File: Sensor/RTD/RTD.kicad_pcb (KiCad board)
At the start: 2 copper layers, 28.6 x 26 mm, 17 parts, among them J1 Conn_02x04_Odd_Even, J2 Conn_01x04_Female, U1 MIC5225, U2 MAX31865

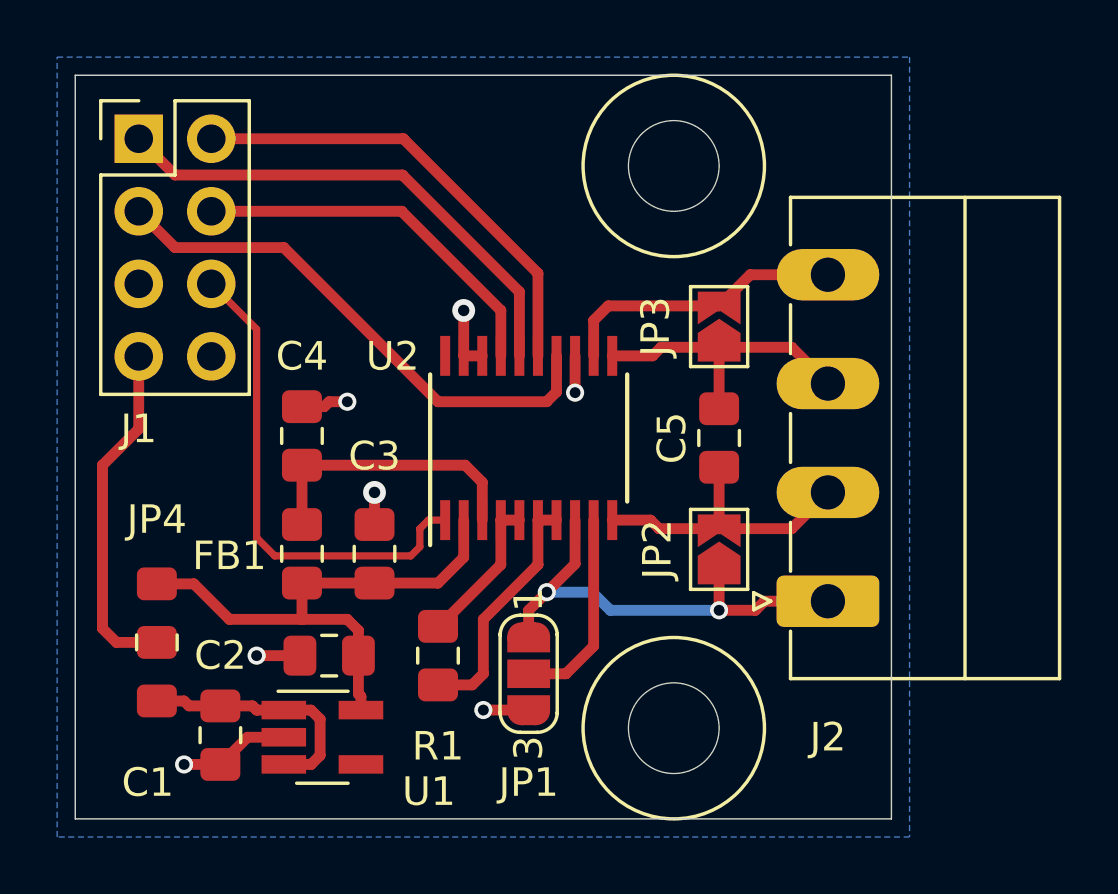
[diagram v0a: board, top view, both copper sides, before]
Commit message: Fix footprint.  Fix wiring for connector.
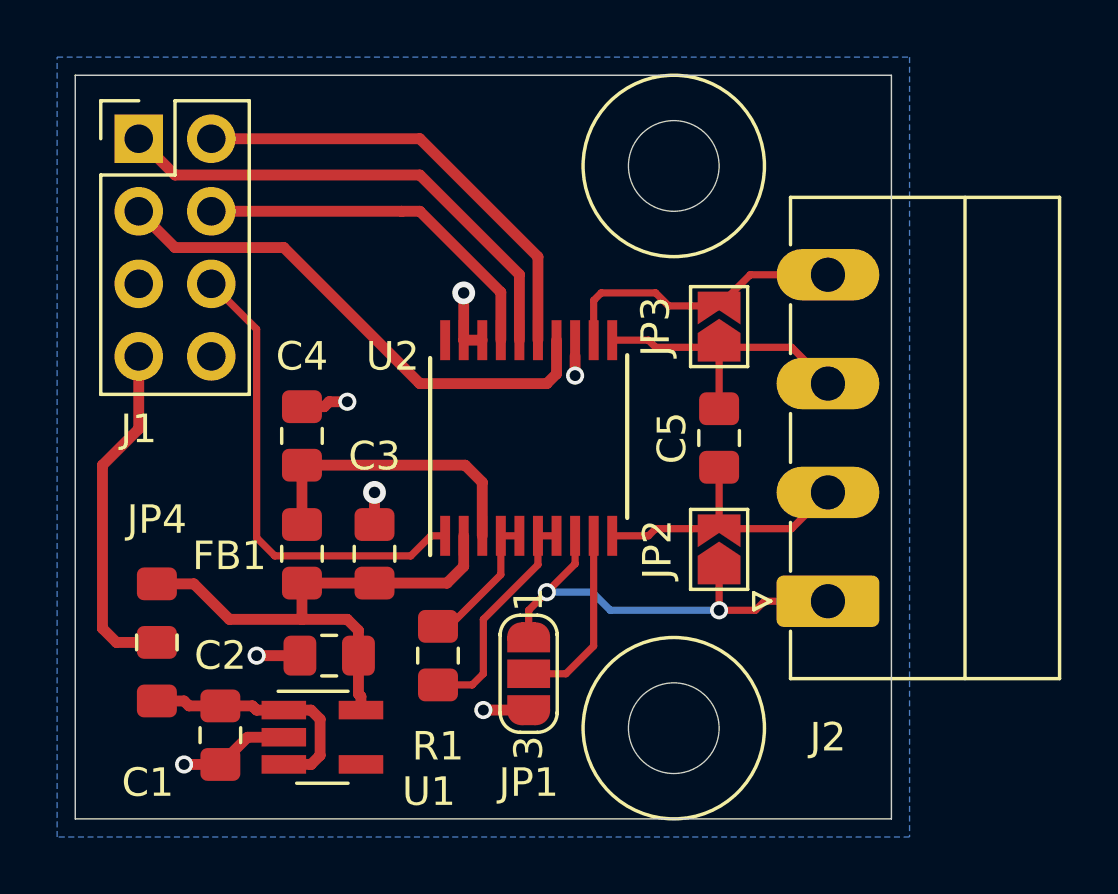
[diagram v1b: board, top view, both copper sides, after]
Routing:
- net /~DRDY: track 17.3 -> 16.7 mm
- net /Vdd: track 9.96 -> 10.5 mm
- net /Force2: track 7.09 -> 6.54 mm
- net /Force+: track 16.4 -> 15.8 mm
- net /Ref-: track 8.57 -> 8.02 mm
- net GND: track 13.3 -> 12.8 mm

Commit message: Updates while making boards.
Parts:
- R1: value R -> 400
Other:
- board text added: "CS SDI NC Vin"
- board text added: "SCLK SDO DRDY GND"
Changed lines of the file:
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@@
   (general
     (thickness 1.6)
-    (drawings 9)
+    (drawings 11)
     (tracks 127)
     (zones 0)
@@
     (pcb_text_size 1.5 1.5)
     (mod_edge_width 0.12)
-    (mod_text_size 1 1)
-    (mod_text_width 0.15)
+    (mod_text_size 0.8 0.8)
+    (mod_text_width 0.12)
     (pad_size 1.524 1.524)
     (pad_drill 0.762)
@@
     (attr smd)
     (fp_text reference U2 (at 2.8575 -4.7625 180) (layer F.SilkS)
-      (effects (font (size 1 1) (thickness 0.15)))
+      (effects (font (size 0.8 0.8) (thickness 0.12)))
     )
     (fp_text value MAX31865 (at 0 4.3 90) (layer F.Fab)
       (effects (font (size 1 1) (thickness 0.15)))
     )
-    (fp_text user %R (at 0 0 90) (layer F.Fab)
-      (effects (font (size 0.8 0.8) (thickness 0.15)))
-    )
-    (fp_line (start -4.1 -3.45) (end 2.8 -3.45) (layer F.SilkS) (width 0.15))
-    (fp_line (start -2.8 3.45) (end 2.9 3.45) (layer F.SilkS) (width 0.15))
+    (fp_line (start -4.1 -3.45) (end 2.8 -3.45) (layer F.SilkS) (width 0.12))
+    (fp_line (start -2.8 3.45) (end 2.9 3.45) (layer F.SilkS) (width 0.12))
     (fp_line (start -4.5 3.55) (end 4.5 3.55) (layer F.CrtYd) (width 0.05))
     (fp_line (start -4.5 -3.55) (end 4.5 -3.55) (layer F.CrtYd) (width 0.05))
@@
     (fp_line (start -1.7 -3.25) (end 2.75 -3.25) (layer F.Fab) (width 0.15))
     (fp_line (start -1.7 -3.25) (end -2.75 -2.25) (layer F.Fab) (width 0.15))
+    (fp_text user %R (at 0 0 90) (layer F.Fab)
+      (effects (font (size 0.8 0.8) (thickness 0.15)))
+    )
     (pad 20 smd rect (at 3.425 -2.925 90) (size 1.4 0.35) (layers F.Cu F.Paste F.Mask))
     (pad 19 smd rect (at 3.425 -2.275 90) (size 1.4 0.35) (layers F.Cu F.Paste F.Mask)
@@
     (tags "phoenix_contact connector MC_01x04_G_3.81mm")
     (fp_text reference J2 (at -4.7625 0 180) (layer F.SilkS)
-      (effects (font (size 1 1) (thickness 0.15)))
+      (effects (font (size 0.8 0.8) (thickness 0.12)))
     )
     (fp_text value Conn_01x04_Female (at 5.72 9.2 90) (layer F.Fab)
@@
     (attr smd)
     (fp_text reference JP4 (at 4.3 0 180) (layer F.SilkS)
-      (effects (font (size 1 1) (thickness 0.15)))
+      (effects (font (size 0.8 0.8) (thickness 0.12)))
     )
     (fp_text value SolderJumper_3_Open (at 0 2.54 90) (layer F.Fab)
@@
     (tags "Through hole pin header THT 2x04 2.54mm double row")
     (fp_text reference J1 (at 0 10.16) (layer F.SilkS)
-      (effects (font (size 1 1) (thickness 0.15)))
+      (effects (font (size 0.8 0.8) (thickness 0.12)))
     )
     (fp_text value Conn_02x04_Odd_Even (at 1.27 9.95) (layer F.Fab)
@@
     (attr virtual)
     (fp_text reference JP1 (at 3.81 0 180) (layer F.SilkS)
-      (effects (font (size 1 1) (thickness 0.15)))
+      (effects (font (size 0.8 0.8) (thickness 0.12)))
     )
     (fp_text value ~ (at 0 1.9 90) (layer F.Fab)
@@
     (fp_arc (start 1.35 -0.3) (end 2.05 -0.3) (angle -90) (layer F.SilkS) (width 0.12))
     (fp_text user 1 (at -2.6 0 90) (layer F.SilkS)
-      (effects (font (size 1 1) (thickness 0.15)))
+      (effects (font (size 0.8 0.8) (thickness 0.12)))
     )
     (fp_text user 3 (at 2.6 0 90) (layer F.SilkS)
-      (effects (font (size 1 1) (thickness 0.15)))
+      (effects (font (size 0.8 0.8) (thickness 0.12)))
     )
     (pad 2 smd rect (at 0 0 270) (size 1 1.5) (layers F.Cu F.Mask)
@@
     (attr smd)
     (fp_text reference U1 (at 3.73 1.905) (layer F.SilkS)
-      (effects (font (size 1 1) (thickness 0.15)))
+      (effects (font (size 0.8 0.8) (thickness 0.12)))
     )
     (fp_text value MIC5225 (at 0 2.9) (layer F.Fab)
@@
     (attr smd)
     (fp_text reference R1 (at 3.175 0 180) (layer F.SilkS)
-      (effects (font (size 1 1) (thickness 0.15)))
-    )
-    (fp_text value R (at 0 1.65 90) (layer F.Fab)
+      (effects (font (size 0.8 0.8) (thickness 0.12)))
+    )
+    (fp_text value 400 (at 0 1.65 90) (layer F.Fab)
       (effects (font (size 1 1) (thickness 0.15)))
     )
@@
     (attr virtual)
     (fp_text reference JP3 (at 0 -2.2225 90) (layer F.SilkS)
-      (effects (font (size 1 1) (thickness 0.15)))
+      (effects (font (size 0.8 0.8) (thickness 0.12)))
     )
     (fp_text value ~ (at 0 1.9 90) (layer F.Fab)
@@
     (attr virtual)
     (fp_text reference JP2 (at 0 -2.1625 90) (layer F.SilkS)
-      (effects (font (size 1 1) (thickness 0.15)))
+      (effects (font (size 0.8 0.8) (thickness 0.12)))
     )
     (fp_text value ~ (at 0 1.9 90) (layer F.Fab)
@@
     (attr smd)
     (fp_text reference FB1 (at -0.0725 -2.54 180) (layer F.SilkS)
-      (effects (font (size 1 1) (thickness 0.15)))
+      (effects (font (size 0.8 0.8) (thickness 0.12)))
     )
     (fp_text value Ferrite_Bead (at 0 1.65 90) (layer F.Fab)
@@
     (attr smd)
     (fp_text reference C5 (at 0 -1.65 90) (layer F.SilkS)
-      (effects (font (size 1 1) (thickness 0.15)))
+      (effects (font (size 0.8 0.8) (thickness 0.12)))
     )
     (fp_text value .1uf (at 0 1.65 90) (layer F.Fab)
@@
     (attr smd)
     (fp_text reference C4 (at -2.785 0 180) (layer F.SilkS)
-      (effects (font (size 1 1) (thickness 0.15)))
+      (effects (font (size 0.8 0.8) (thickness 0.12)))
     )
     (fp_text value .1uf (at 0 1.65 90) (layer F.Fab)
@@
     (attr smd)
     (fp_text reference C3 (at 3.42 0) (layer F.SilkS)
-      (effects (font (size 1 1) (thickness 0.15)))
+      (effects (font (size 0.8 0.8) (thickness 0.12)))
     )
     (fp_text value .1uf (at 0 1.65 90) (layer F.Fab)
@@
     (attr smd)
     (fp_text reference C2 (at 3.81 0) (layer F.SilkS)
-      (effects (font (size 1 1) (thickness 0.15)))
+      (effects (font (size 0.8 0.8) (thickness 0.12)))
     )
     (fp_text value "2.2uf 300mOhm ESR" (at 0 1.65) (layer F.Fab)
@@
     (attr smd)
     (fp_text reference C1 (at 1.66 2.54 180) (layer F.SilkS)
-      (effects (font (size 1 1) (thickness 0.15)))
+      (effects (font (size 0.8 0.8) (thickness 0.12)))
     )
     (fp_text value 1.0uf (at 0 1.65 90) (layer F.Fab)
@@
     )
   )
+  (gr_text "SCLK\nSDO\nDRDY\nGND" (at 106.045 61.9125) (layer F.SilkS)
+    (effects (font (size 0.8 0.8) (thickness 0.12)) (justify left))
+  )
+  (gr_text "CS\nSDI\nNC\nVin" (at 103.505 61.9125) (layer F.SilkS)
+    (effects (font (size 0.8 0.8) (thickness 0.12)) (justify left))
+  )
   (dimension 19.685 (width 0.15) (layer Dwgs.User)
